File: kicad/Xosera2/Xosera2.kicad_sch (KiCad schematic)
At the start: 0 parts

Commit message: Make a start on placement
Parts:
- added H1, H2, H3, H4: MountingHole, MountingHole:MountingHole_3.2mm_M3_Pad_Via, symbol UPduino_v3.0:Mechanical_MountingHole
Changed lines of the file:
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@@
   (title_block
     (title "Xosera rosco_m68k daughterboard")
-    (date "2023-12-21")
+    (date "2024-02-08")
     (rev "0")
     (company "The Really Old-School Company Limited & XarkLabs")
@@
     (effects (font (size 2 2)) (justify left bottom))
   )
+  (symbol (lib_id "UPduino_v3.0:Mechanical_MountingHole") (at 42.545 175.895 0) (unit 1)
+    (in_bom yes) (on_board yes) (dnp no)
+    (property "Reference" "H2" (at 45.085 174.7266 0)
+      (effects (font (size 1.27 1.27)) (justify left))
+    )
+    (property "Value" "MountingHole" (at 45.085 177.038 0)
+      (effects (font (size 1.27 1.27)) (justify left))
+    )
+    (property "Footprint" "MountingHole:MountingHole_3.2mm_M3_Pad_Via" (at 42.545 175.895 0)
+      (effects (font (size 1.27 1.27)) hide)
+    )
+    (property "Datasheet" "~" (at 42.545 175.895 0)
+      (effects (font (size 1.27 1.27)) hide)
+    )
+    (instances
+      (project "UPduino_v3.0"
+        (path "/0a0223e0-d287-426a-af6a-2d9597a86d6d"
+          (reference "H2") (unit 1)
+        )
+      )
+      (project "Xosera2"
+        (path "/e3ab5ddd-7cd3-46c7-91c9-5fc78e7ae4ac/542e2bbe-89ea-4794-ae61-2e32ec6db8f5"
+          (reference "H4") (unit 1)
+        )
+        (path "/e3ab5ddd-7cd3-46c7-91c9-5fc78e7ae4ac"
+          (reference "H4") (unit 1)
+        )
+      )
+    )
+  )
+  (symbol (lib_id "UPduino_v3.0:Mechanical_MountingHole") (at 24.13 185.42 0) (unit 1)
+    (in_bom yes) (on_board yes) (dnp no)
+    (property "Reference" "H3" (at 26.67 184.2516 0)
+      (effects (font (size 1.27 1.27)) (justify left))
+    )
+    (property "Value" "MountingHole" (at 26.67 186.563 0)
+      (effects (font (size 1.27 1.27)) (justify left))
+    )
+    (property "Footprint" "MountingHole:MountingHole_3.2mm_M3_Pad_Via" (at 24.13 185.42 0)
+      (effects (font (size 1.27 1.27)) hide)
+    )
+    (property "Datasheet" "~" (at 24.13 185.42 0)
+      (effects (font (size 1.27 1.27)) hide)
+    )
+    (instances
+      (project "UPduino_v3.0"
+        (path "/0a0223e0-d287-426a-af6a-2d9597a86d6d"
+          (reference "H3") (unit 1)
+        )
+      )
+      (project "Xosera2"
+        (path "/e3ab5ddd-7cd3-46c7-91c9-5fc78e7ae4ac/542e2bbe-89ea-4794-ae61-2e32ec6db8f5"
+          (reference "H2") (unit 1)
+        )
+        (path "/e3ab5ddd-7cd3-46c7-91c9-5fc78e7ae4ac"
+          (reference "H2") (unit 1)
+        )
+      )
+    )
+  )
+  (symbol (lib_id "UPduino_v3.0:Mechanical_MountingHole") (at 41.91 185.42 0) (unit 1)
+    (in_bom yes) (on_board yes) (dnp no)
+    (property "Reference" "H4" (at 44.45 184.2516 0)
+      (effects (font (size 1.27 1.27)) (justify left))
+    )
+    (property "Value" "MountingHole" (at 44.45 186.563 0)
+      (effects (font (size 1.27 1.27)) (justify left))
+    )
+    (property "Footprint" "MountingHole:MountingHole_3.2mm_M3_Pad_Via" (at 41.91 185.42 0)
+      (effects (font (size 1.27 1.27)) hide)
+    )
+    (property "Datasheet" "~" (at 41.91 185.42 0)
+      (effects (font (size 1.27 1.27)) hide)
+    )
+    (instances
+      (project "UPduino_v3.0"
+        (path "/0a0223e0-d287-426a-af6a-2d9597a86d6d"
+          (reference "H4") (unit 1)
+        )
+      )
+      (project "Xosera2"
+        (path "/e3ab5ddd-7cd3-46c7-91c9-5fc78e7ae4ac/542e2bbe-89ea-4794-ae61-2e32ec6db8f5"
+          (reference "H3") (unit 1)
+        )
+        (path "/e3ab5ddd-7cd3-46c7-91c9-5fc78e7ae4ac"
+          (reference "H3") (unit 1)
+        )
+      )
+    )
+  )
+  (symbol (lib_id "UPduino_v3.0:Mechanical_MountingHole") (at 24.13 176.53 0) (unit 1)
+    (in_bom yes) (on_board yes) (dnp no)
+    (property "Reference" "H1" (at 26.67 175.3616 0)
+      (effects (font (size 1.27 1.27)) (justify left))
+    )
+    (property "Value" "MountingHole" (at 26.67 177.673 0)
+      (effects (font (size 1.27 1.27)) (justify left))
+    )
+    (property "Footprint" "MountingHole:MountingHole_3.2mm_M3_Pad_Via" (at 24.13 176.53 0)
+      (effects (font (size 1.27 1.27)) hide)
+    )
+    (property "Datasheet" "~" (at 24.13 176.53 0)
+      (effects (font (size 1.27 1.27)) hide)
+    )
+    (instances
+      (project "UPduino_v3.0"
+        (path "/0a0223e0-d287-426a-af6a-2d9597a86d6d"
+          (reference "H1") (unit 1)
+        )
+      )
+      (project "Xosera2"
+        (path "/e3ab5ddd-7cd3-46c7-91c9-5fc78e7ae4ac/542e2bbe-89ea-4794-ae61-2e32ec6db8f5"
+          (reference "H1") (unit 1)
+        )
+        (path "/e3ab5ddd-7cd3-46c7-91c9-5fc78e7ae4ac"
+          (reference "H1") (unit 1)
+        )
+      )
+    )
+  )
   (sheet (at 30.48 62.23) (size 30.48 73.66) (fields_autoplaced)

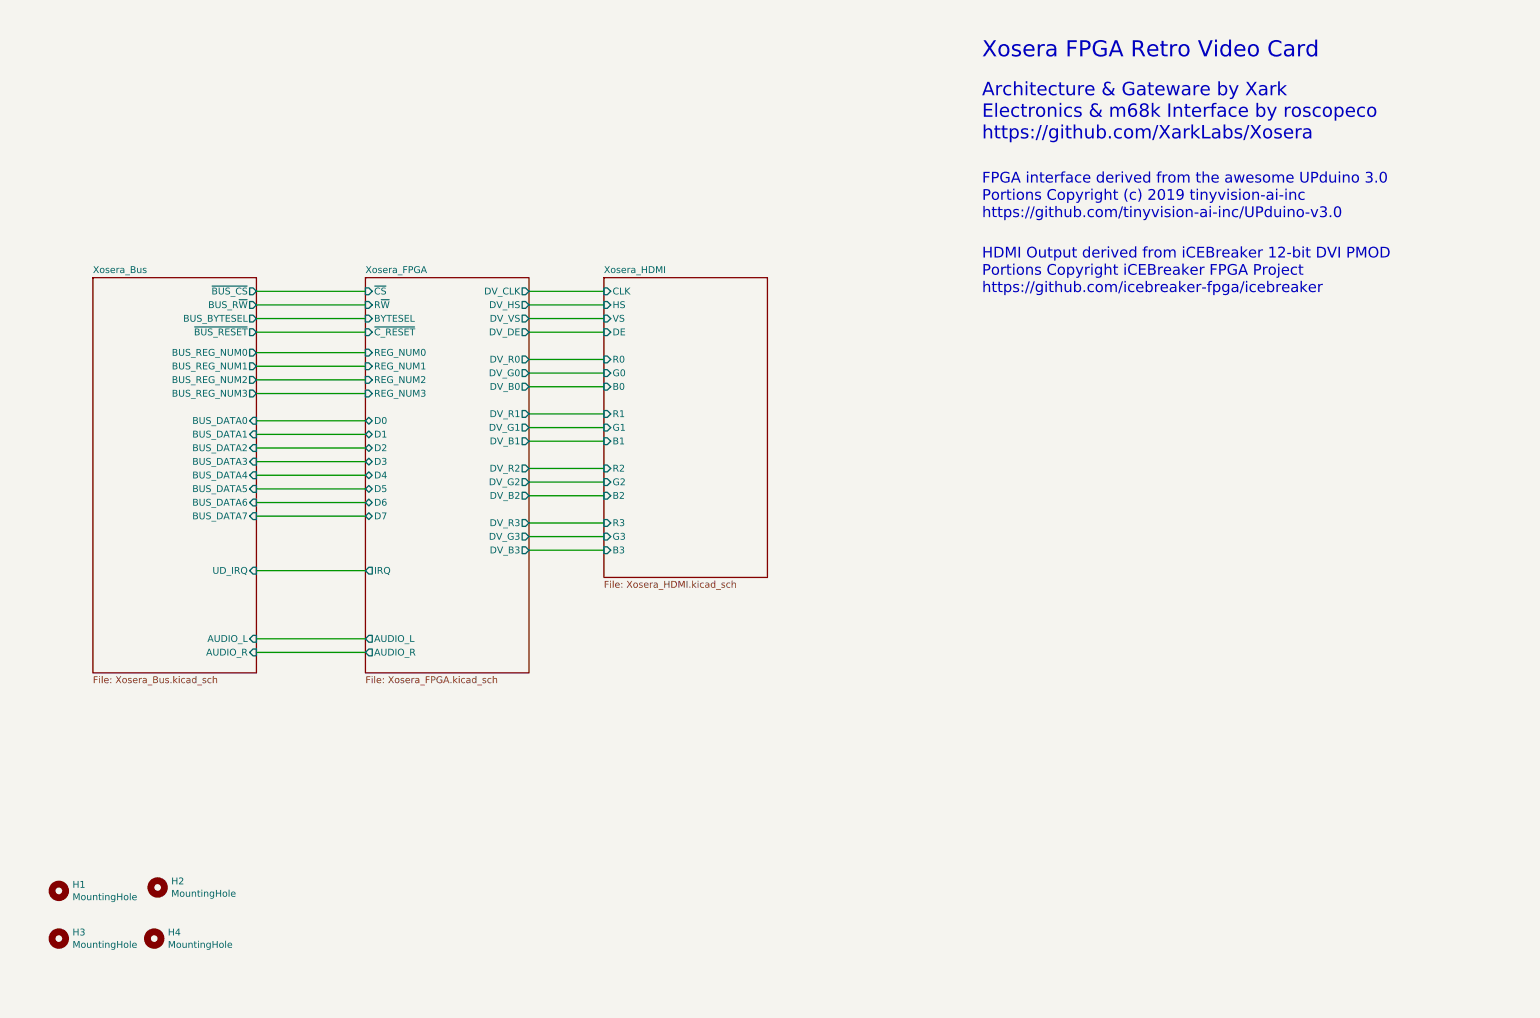
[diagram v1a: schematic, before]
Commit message: Replace all GALs with one 1504
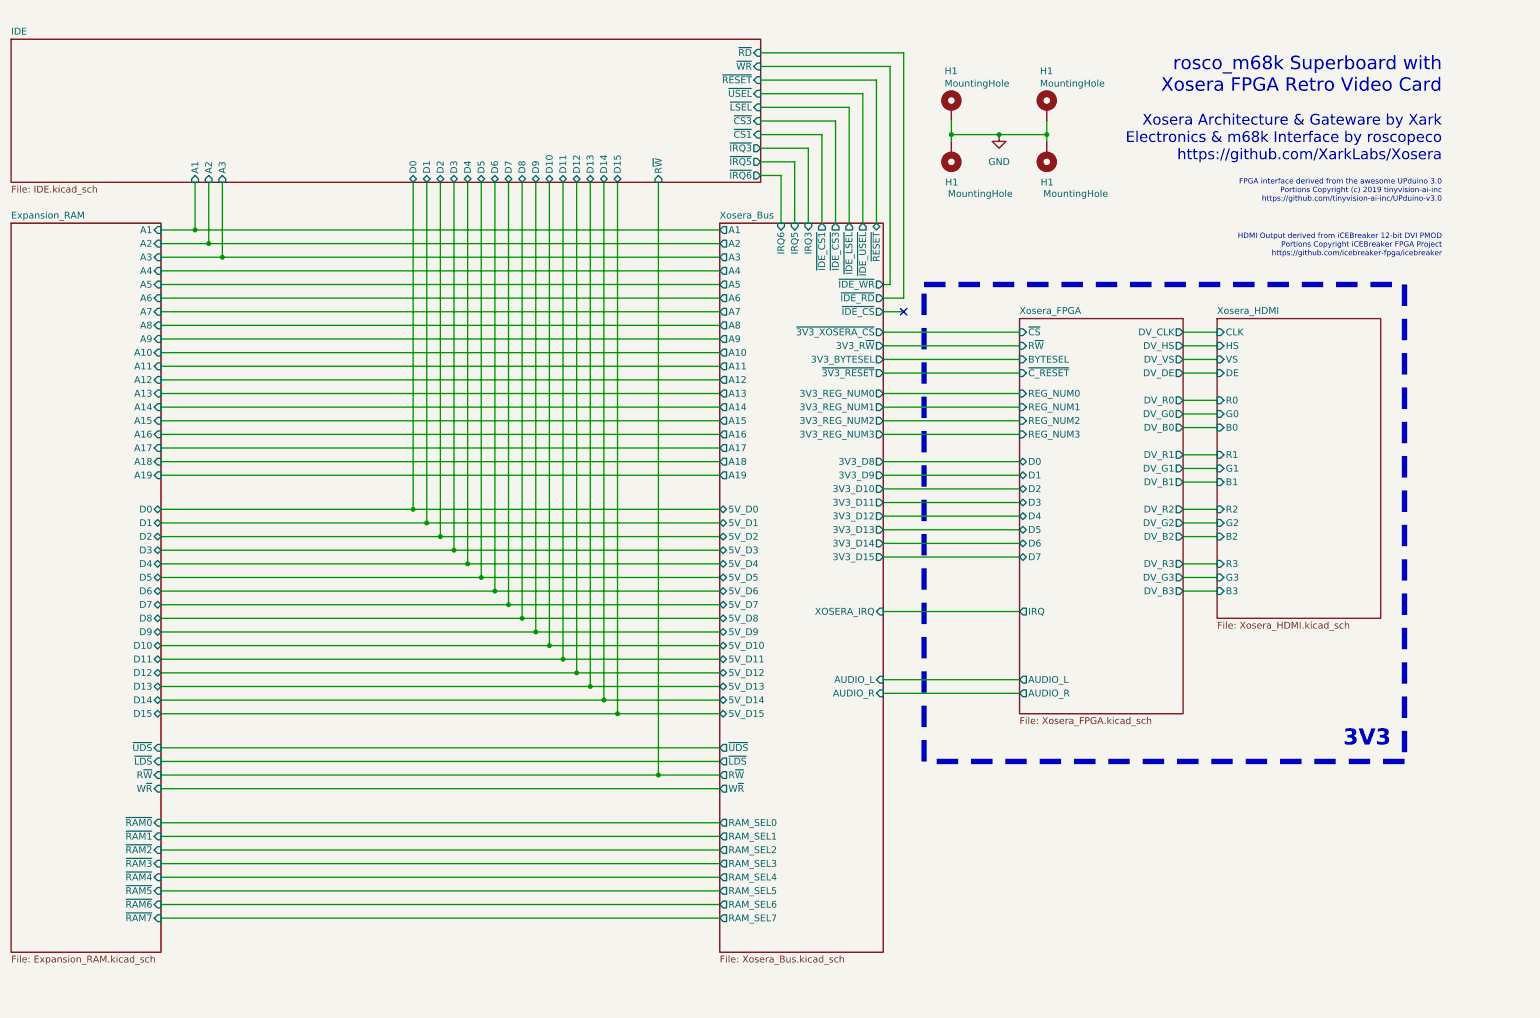
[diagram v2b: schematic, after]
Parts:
- removed H2, H3, H4: MountingHole, MountingHole:MountingHole_3.2mm_M3_Pad_Via, symbol UPduino_v3.0:Mechanical_MountingHole
- added H1 (x3): MountingHole, MountingHole:MountingHole_3.2mm_M3_Pad_Via, symbol Mechanical:MountingHole_Pad
- H1: symbol UPduino_v3.0:Mechanical_MountingHole -> Mechanical:MountingHole_Pad
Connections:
- new net GND: H1.1, H1.1, H1.1, H1.1
- no-connect marks 0 -> 1
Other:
- added sheet Expansion_RAM (Expansion_RAM.kicad_sch)
- added sheet IDE (IDE.kicad_sch)
- sheet Xosera_Bus ports: added 3V3_BYTESEL, 3V3_D10, 3V3_D11, 3V3_D12, 3V3_D13, 3V3_D14, 3V3_D15, 3V3_D8, 3V3_D9, 3V3_REG_NUM0, 3V3_REG_NUM1, 3V3_REG_NUM2, 3V3_REG_NUM3, 3V3_R~{W}, 5V_D0, 5V_D1, 5V_D10, 5V_D11, 5V_D12, 5V_D13, 5V_D14, 5V_D15, 5V_D2, 5V_D3, 5V_D4, 5V_D5, 5V_D6, 5V_D7, 5V_D8, 5V_D9, A1, A10, A11, A12, A13, A14, A15, A16, A17, A18, A19, A2, A3, A4, A5, A6, A7, A8, A9, IRQ3, IRQ5, IRQ6, RAM_SEL0, RAM_SEL1, RAM_SEL2, RAM_SEL3, RAM_SEL4, RAM_SEL5, RAM_SEL6, RAM_SEL7, R~{W}, W~{R}, XOSERA_IRQ, ~{3V3_RESET}, ~{3V3_XOSERA_CS}, ~{IDE_CS1}, ~{IDE_CS3}, ~{IDE_CS}, ~{IDE_LSEL}, ~{IDE_RD}, ~{IDE_USEL}, ~{IDE_WR}, ~{LDS}, ~{RESET}, ~{UDS}; removed BUS_BYTESEL, BUS_DATA0, BUS_DATA1, BUS_DATA2, BUS_DATA3, BUS_DATA4, BUS_DATA5, BUS_DATA6, BUS_DATA7, BUS_REG_NUM0, BUS_REG_NUM1, BUS_REG_NUM2, BUS_REG_NUM3, BUS_R~{W}, UD_IRQ, ~{BUS_CS}, ~{BUS_RESET}
- note added: "3V3"
- note added: "Xosera Architecture & Gateware by Xark Electronics & m68k Interface by roscopeco https://github.com/XarkLabs/Xosera"
- note added: "rosco_m68k Superboard with Xosera FPGA Retro Video Card"
- note removed: "Architecture & Gateware by Xark Electronics & m68k Interface by roscopeco https://github.com/XarkLabs/Xosera"
- note removed: "Xosera FPGA Retro Video Card"
- title: Xosera rosco_m68k daughterboard -> rosco_m68k Super Board

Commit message: Fix ERC (mostly) and sort out footprints etc
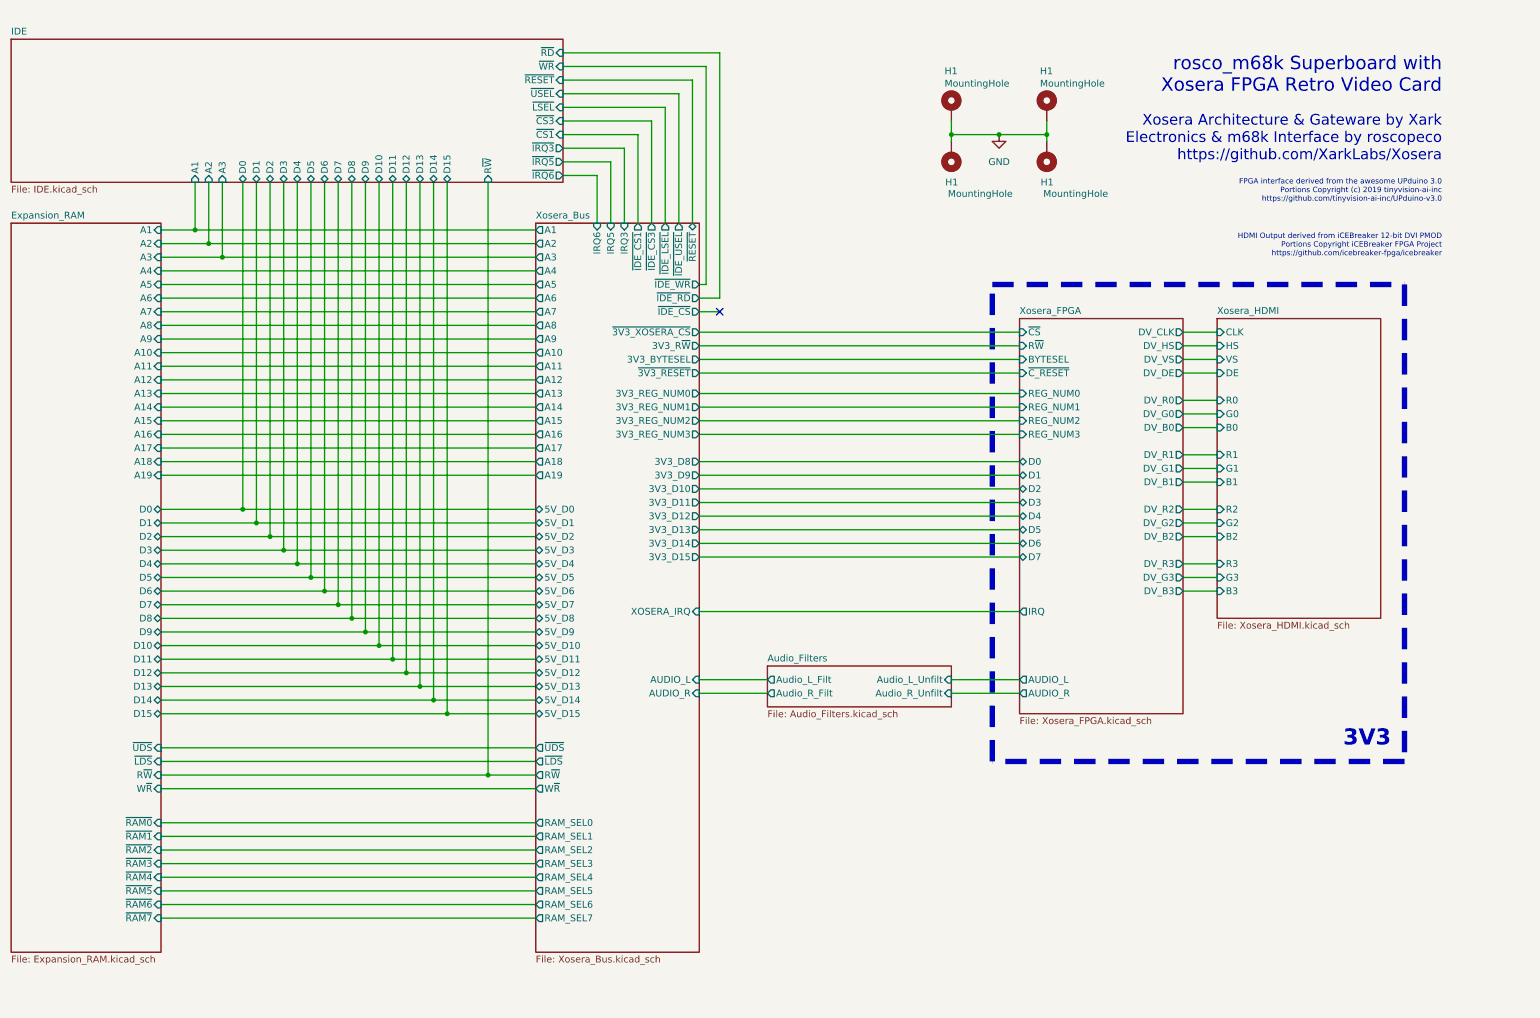
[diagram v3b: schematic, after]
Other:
- added sheet Audio_Filters (Audio_Filters.kicad_sch)

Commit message: Initial layout, delete some useless things
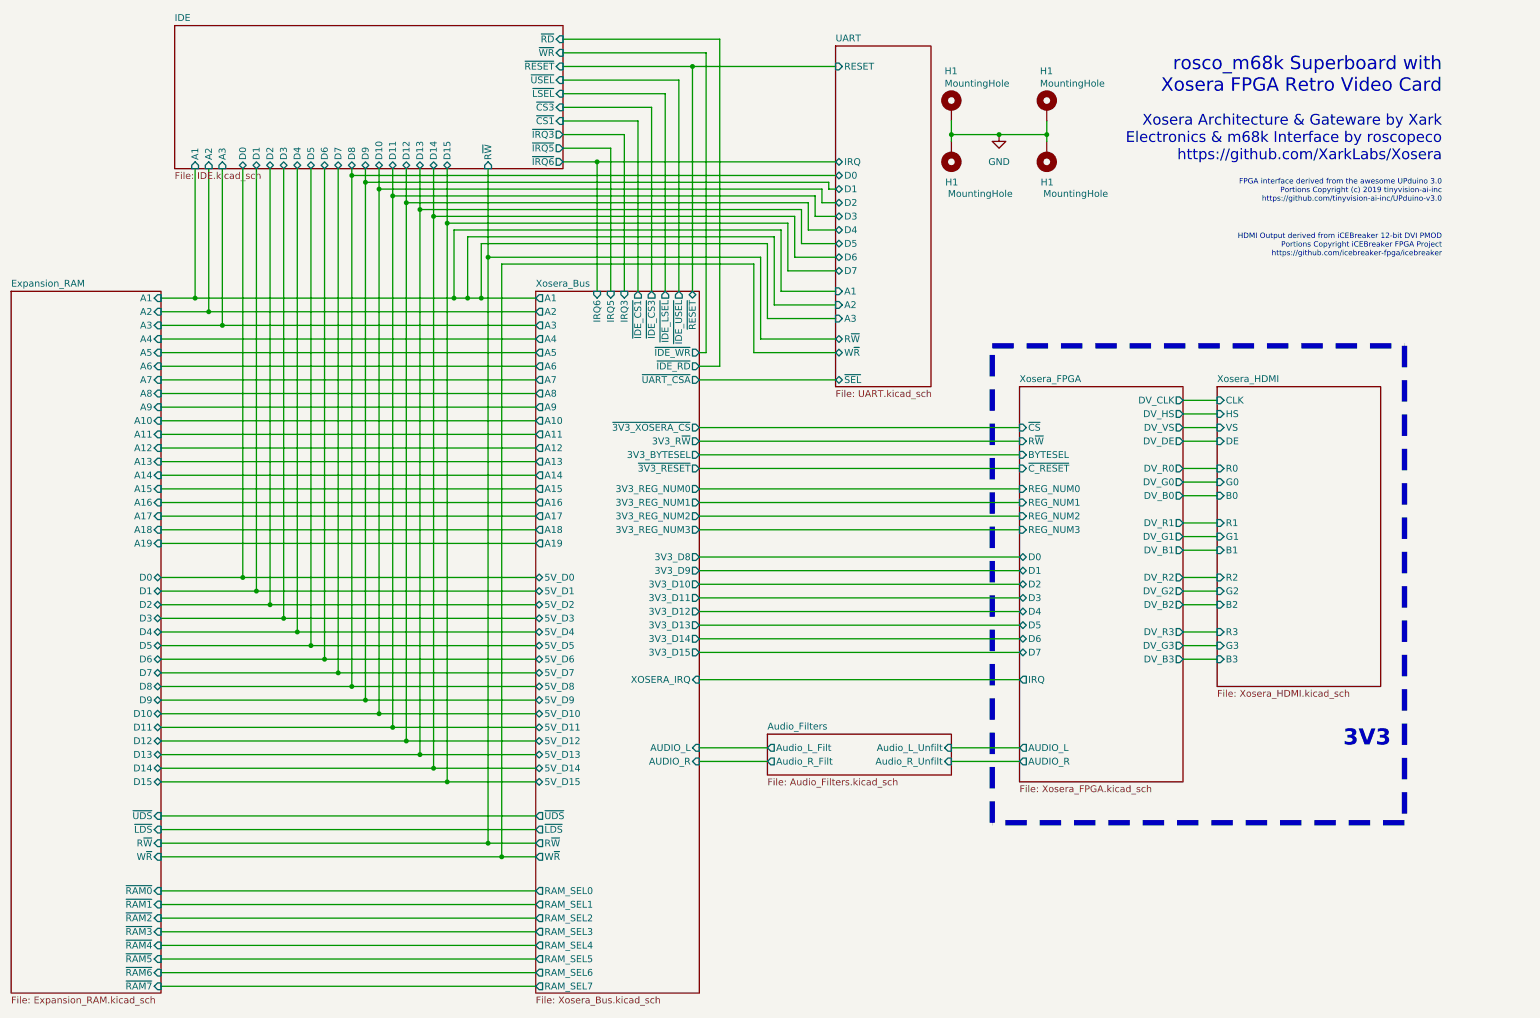
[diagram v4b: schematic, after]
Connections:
- no-connect marks 1 -> 0
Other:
- added sheet UART (UART.kicad_sch)
- sheet Xosera_Bus ports: added ~{UART_CSA}; removed ~{IDE_CS}
